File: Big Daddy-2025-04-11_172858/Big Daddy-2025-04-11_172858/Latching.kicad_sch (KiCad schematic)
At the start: 11 parts, among them J14 BMS Button, J2 IMD Button, K2 G5V-1, K3 G5V-2

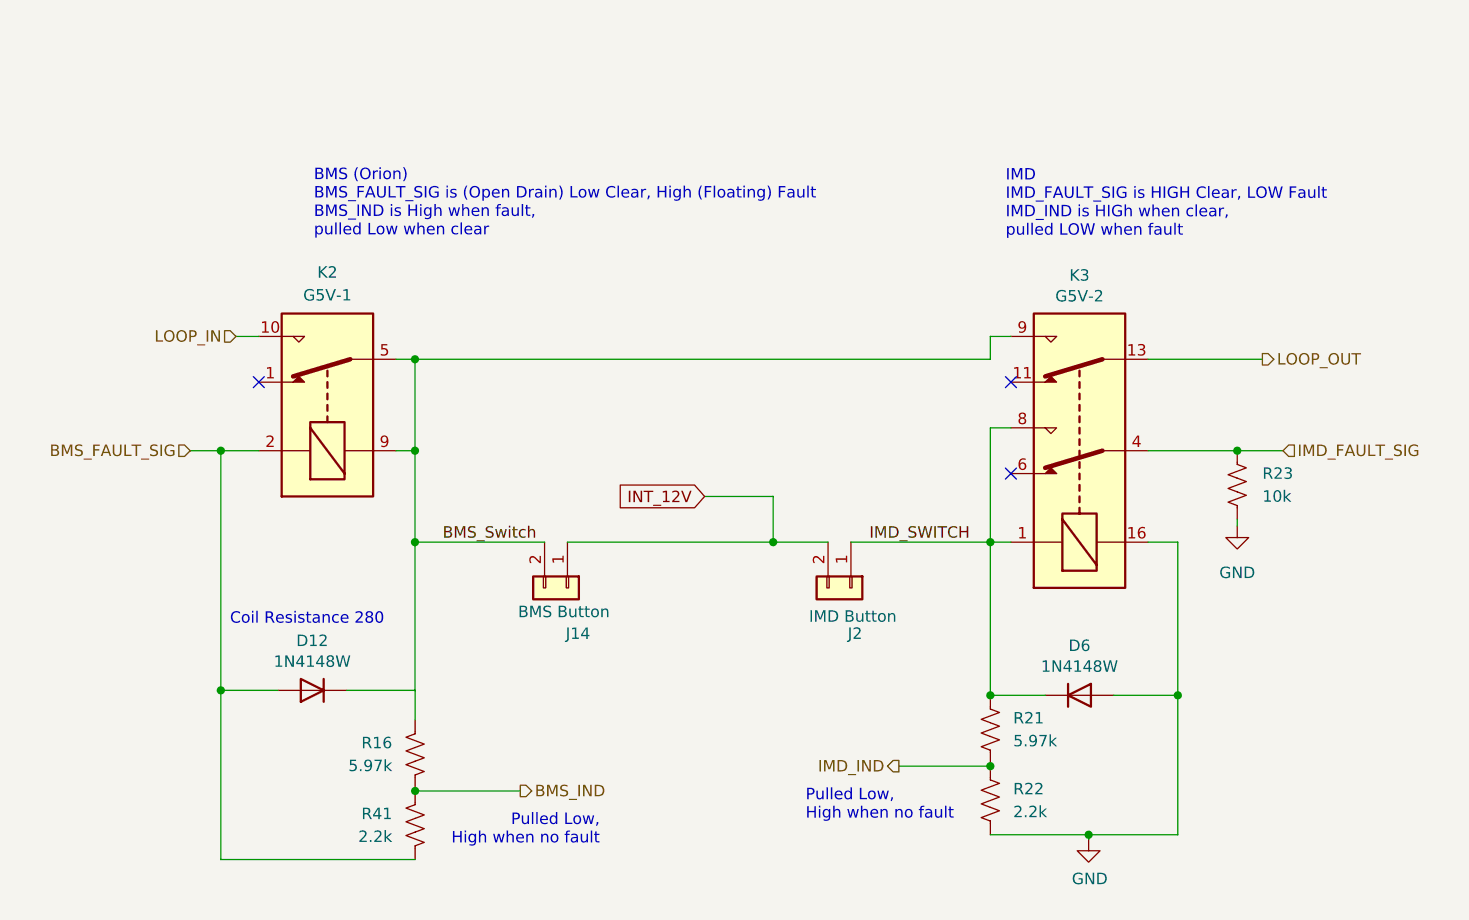
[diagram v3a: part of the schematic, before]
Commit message: BMS Indicator
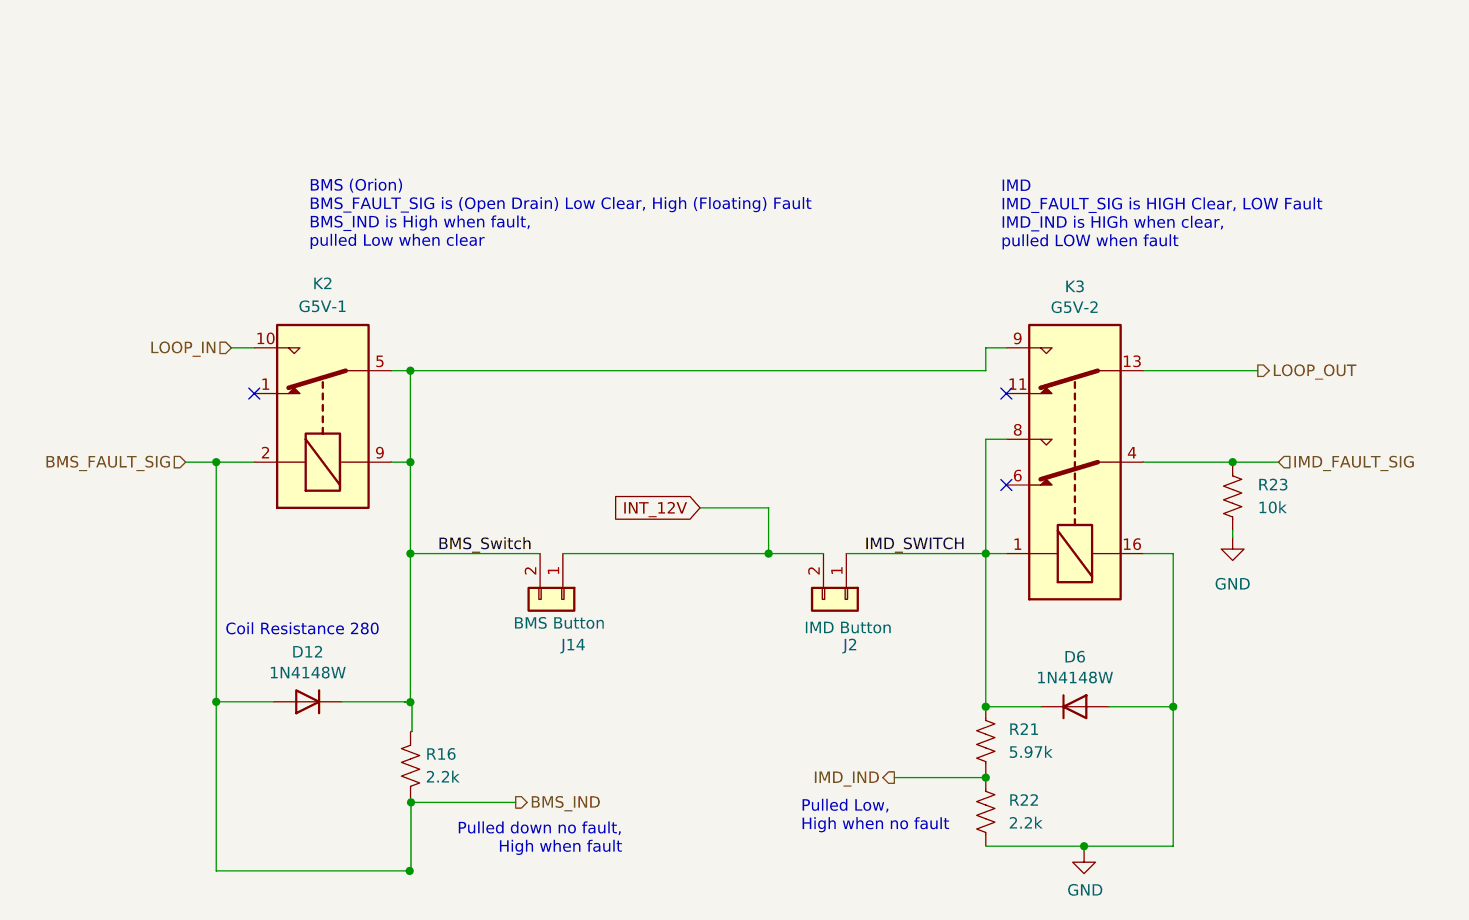
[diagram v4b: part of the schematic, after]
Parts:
- removed R41: 2.2k, Resistor_SMD:R_0603_1608Metric_Pad0.98x0.95mm_HandSolder, symbol Device:R_US
- R16: value 5.97k -> 2.2k
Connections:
- net BMS_IND is gone; now on net BMS_FAULT_SIG: R16.2
- net BMS_Switch: now also D12.1 (K), R16.1
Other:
- note added: "Pulled down no fault, High when fault"
- moved on the sheet: D12, D6, J14, J2, K2, K3, R16, R21, R22, R23

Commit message: all the bs
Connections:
- net LOOP_IN is gone; now on net 12V_in: K2.10
- net INT_12V renamed 12V_in
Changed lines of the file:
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@@
-	(wire
-		(pts
-			(xy 137.922 78.74) (xy 145.542 78.74)
-		)
-		(stroke
-			(width 0)
-			(type default)
-		)
-	)
 	(wire
 		(pts
@@
 	(wire
 		(pts
+			(xy 137.16 78.74) (xy 145.542 78.74)
+		)
+		(stroke
+			(width 0)
+			(type default)
+		)
+	)
+	(wire
+		(pts
 			(xy 122.682 83.82) (xy 145.542 83.82)
 		)
@@
 	(wire
 		(pts
+			(xy 85.09 60.96) (xy 88.392 60.96)
+		)
+		(stroke
+			(width 0)
+			(type default)
+		)
+	)
+	(wire
+		(pts
 			(xy 169.672 63.5) (xy 169.672 60.96)
 		)
@@
 		(pts
 			(xy 84.1684 73.66) (xy 88.392 73.66)
-		)
-		(stroke
-			(width 0)
-			(type default)
-		)
-	)
-	(wire
-		(pts
-			(xy 85.852 60.96) (xy 88.392 60.96)
 		)
 		(stroke
@@
 			)
 			(justify right bottom)
-		)
-	)
-	(global_label "INT_12V"
-		(shape input)
-		(at 137.922 78.74 180)
-		(fields_autoplaced yes)
-		(effects
-			(font
-				(size 1.27 1.27)
-			)
-			(justify right)
-		)
-		(property "Intersheetrefs" "${INTERSHEET_REFS}"
-			(at 128.2197 78.8194 0)
-			(effects
-				(font
-					(size 1.27 1.27)
-				)
-				(justify right)
-				(hide yes)
-			)
 		)
 	)
@@
 		)
 	)
-	(hierarchical_label "LOOP_IN"
+	(hierarchical_label "12V_in"
 		(shape input)
-		(at 85.852 60.96 180)
+		(at 85.09 60.96 180)
 		(effects
 			(font
@@
 		)
 	)
+	(hierarchical_label "12V_in"
+		(shape input)
+		(at 137.16 78.74 180)
+		(effects
+			(font
+				(size 1.27 1.27)
+			)
+			(justify right)
+		)
+	)
